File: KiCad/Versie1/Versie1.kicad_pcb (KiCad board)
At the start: 2 copper layers, 64 x 50 mm, 78 parts, among them IC1 MCP73831T-2ATI_OT, IC2 AP9221SA-CC-HAC-7, IC3 ISL91107IRTNZ-T7A, J1 Leftover, J2 USB_C_Receptacle_USB2.0, J3 JTAG, J4 Programmer, J5 SPI, J6 I2C, J7 BOOT, J8 Screw_Terminal_01x02, J9 Screw_Terminal_01x02, Q1 Q_NMOS_GSD, Q2 Q_NMOS_GSD, Q3 Q_NMOS_GSD, Q4 Q_NMOS_GSD, U1 ESP32-WROOM-32, Y1 32.768kHz

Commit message: H2, C13, C14 aangepast
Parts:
- moved H2 13.5 mm to (109.5, 87.6)
- moved C13 4.49 mm to (113.8, 87.1)
- moved JP5 3.59 mm to (96.0, 89.7)
- moved JP3 3.56 mm to (104.4, 89.3)
- moved JP4 3.53 mm to (100.7, 89.7)
- moved C14 3.26 mm to (113.8, 83.7)
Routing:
- net SPI_MOSI: track 56.1 -> 46.1 mm
- net I2C_SDA: track 38.4 -> 32.7 mm
- net SPI_MISO: track 33.4 -> 28.5 mm
- net I2C_SCL: track 40.5 -> 36.4 mm
- net SPI_CLK: track 24.0 -> 20.4 mm
- net GND: track 74.7 -> 71.5 mm, vias 52 -> 48
- net SCL\SCK\RX: track 49.8 -> 53.1 mm
- net +3V3: track 252.6 -> 249.9 mm
- net +BATT: track 137.2 -> 135.7 mm, vias 2 -> 3
- net uC_SENSE: track 41.6 -> 42.9 mm
- net SDA\MISO\TX: track 42.4 -> 43.7 mm

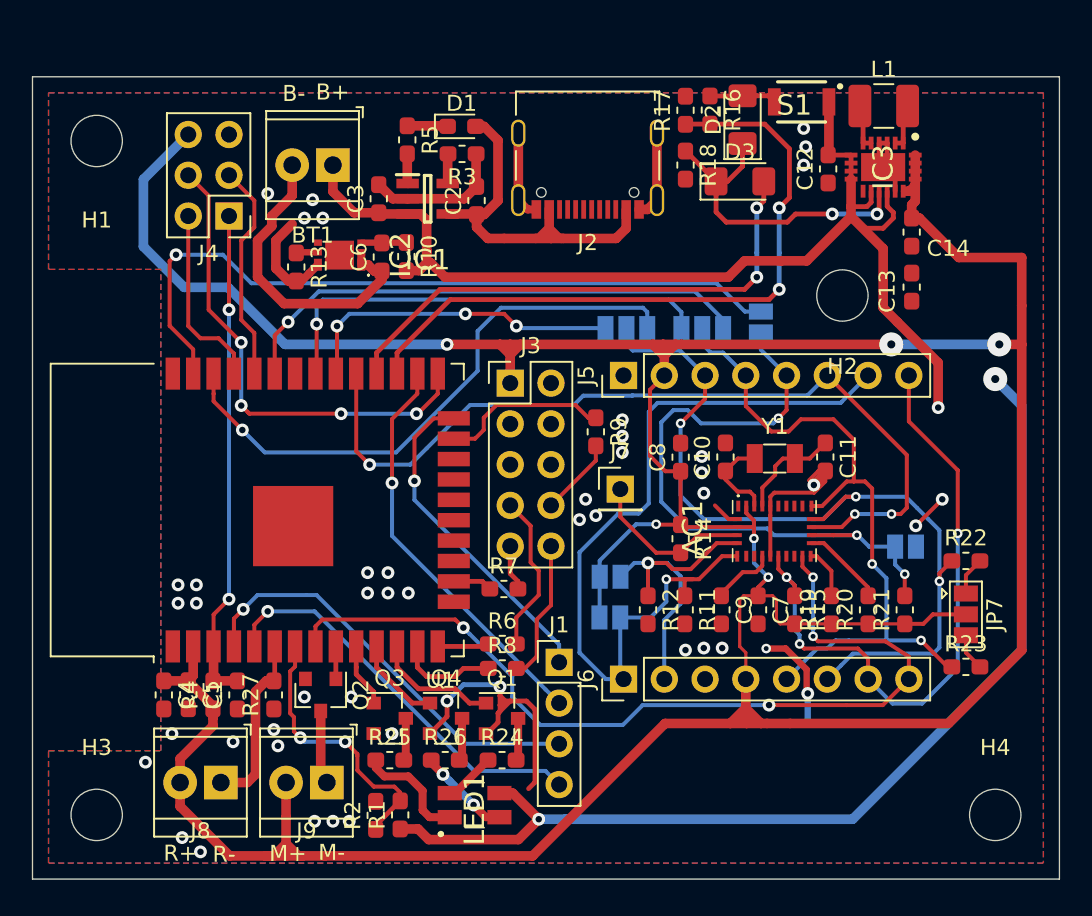
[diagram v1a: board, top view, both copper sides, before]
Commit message: 5x6cm PCB en silkscreen update
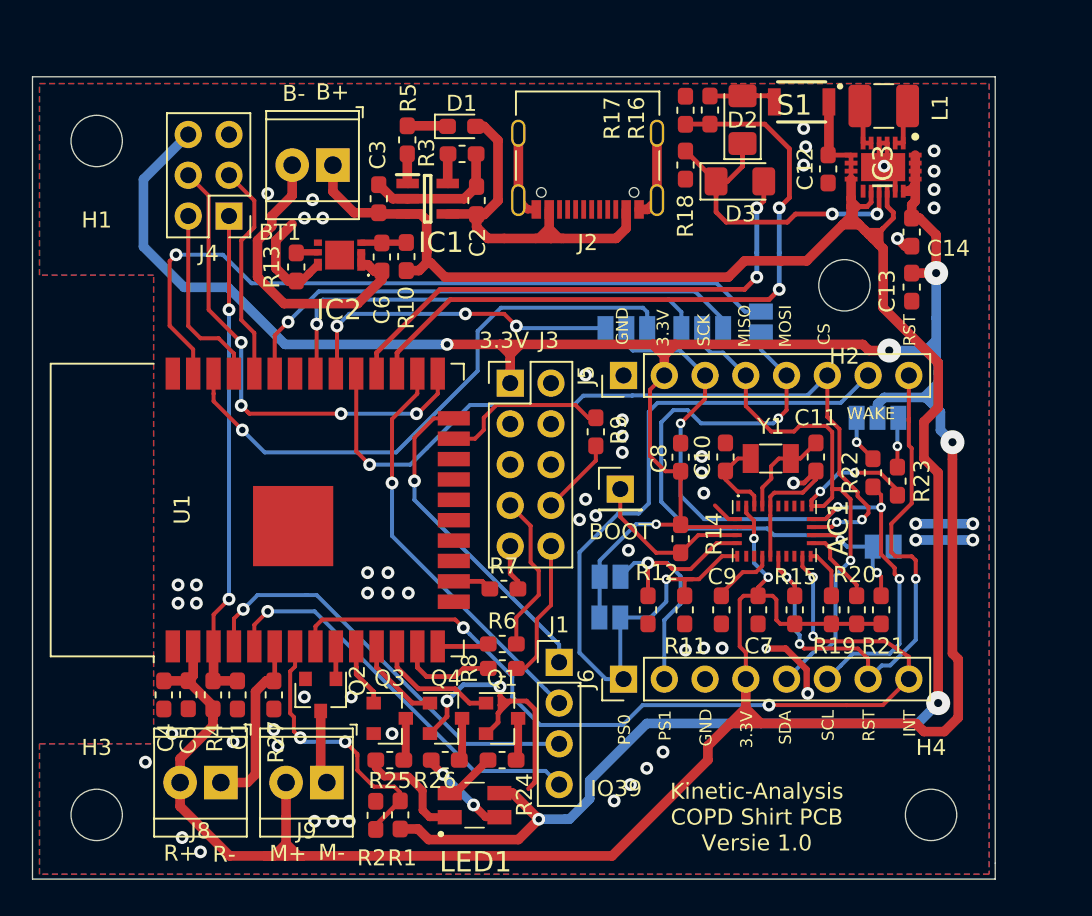
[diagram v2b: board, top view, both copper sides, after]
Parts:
- JP7: moved to B.Cu
- moved JP7 13.4 mm to (111.7, 95.2), turned to 0 degrees
- moved R23 12.3 mm to (112.9, 99.2), turned to 90 degrees
- moved R22 7.98 mm to (111.4, 98.7), turned to 90 degrees
- moved H4 4.00 mm to (115.0, 120.0)
- moved R21 1.47 mm to (111.9, 107.2)
- moved JP6 1.40 mm to (112.0, 103.3)
- moved R20 0.71 mm to (110.4, 107.2)
- moved H2 0.65 mm to (109.6, 87.0)
- moved C11 0.59 mm to (107.8, 97.7)
- moved Y1 0.25 mm to (105.0, 97.8)
- renumbered J7 to BOOT
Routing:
- net SCL\SCK\RX: track 53.1 -> 46.1 mm, vias 3 -> 4
- net RST: track 39.9 -> 35.8 mm
- net +3V3: track 249.9 -> 245.9 mm, vias 6 -> 7
- net SDA\MISO\TX: track 43.7 -> 40.2 mm, vias 2 -> 3
- net SPI_CS: track 53.6 -> 50.4 mm
- net GND: track 71.5 -> 74.1 mm, vias 48 -> 62
- net ADDR\MOSI: track 41.2 -> 38.8 mm
- net +BATT: track 135.7 -> 137.5 mm, vias 3 -> 2
- net Net-(JP7-Pad3): track 2.39 -> 3.10 mm, vias 0 -> 1
- net Net-(JP7-Pad1): track 2.39 -> 2.97 mm, vias 0 -> 1
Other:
- board size 64 x 50 mm -> 60 x 50 mm
- rule trace_min: 0.1 -> 0.25
- rule via_min_size: 0.4 -> 0.3
- board text added: "3.3V"
- board text added: "CS"
- board text added: "GND"
- board text added: "INT"
- board text added: "IO39"
- board text added: "Kinetic-Analysis COPD Shirt PCB Versie 1.0"
- board text added: "MISO"
- board text added: "MOSI"
- board text added: "PS0"
- board text added: "PS1"
- board text added: "RST"
- board text added: "SCK"
- board text added: "SCL"
- board text added: "SDA"
- board text added: "WAKE"

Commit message: BOM Lijst
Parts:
- removed the IC1 at (83.6, 81.6)
- removed the R3 at (85.8, 78.8)
- removed the R5 at (82.4, 77.9)
- added R8: 470, Resistor_SMD:R_0603_1608Metric_Pad1.05x0.95mm_HandSolder, F.Cu at (85.2, 80.8)
- added R9: 2k, Resistor_SMD:R_0603_1608Metric_Pad1.05x0.95mm_HandSolder, F.Cu at (85.2, 82.3)
- added U2: , Versie1_FootprintLib:MCP73831T-2ATI&slash_MC, F.Cu at (84.6, 78.0)
- C2, C3: value 4,7uF -> 4.7uF
- J2: value USB_C_Receptacle_USB2.0 -> USB_C_Receptacle_USB3.0
- moved C2 6.72 mm to (85.7, 75.1), turned to 0 degrees
- moved C3 4.64 mm to (82.7, 77.5), turned to 270 degrees
- moved D1 1.25 mm to (86.6, 78.0), turned to 90 degrees
- renumbered C7 to C6, C8 to C7, C6 to C8, IC2 to IC1, IC3 to IC2, BOOT to J7, R11 to R10, R12 to R11, R10 to R12, R14 to R13, R15 to R14, R13 to R15, R19 to R18, R18 to R19, R27 to R24, R24 to R25, R25 to R26, R26 to R27, R4 to R3, R6 to R4, R7 to R5, R8 to R6, R9 to R7
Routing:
- net +BATT: track 137.5 -> 148.4 mm
- net Net-(R9-Pad1): track 0.00 -> 3.66 mm
- net GND: track 74.1 -> 71.5 mm, vias 62 -> 64
- net Net-(IC1-Pad1): track 1.85 -> 0.00 mm
- net Net-(IC1-Pad5) (its old number): track 1.85 -> 0.00 mm
- net Net-(R8-Pad2): track 0.00 -> 1.61 mm
- net +5V: track 26.1 -> 25.0 mm
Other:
- board text added: "ESP_TXD"

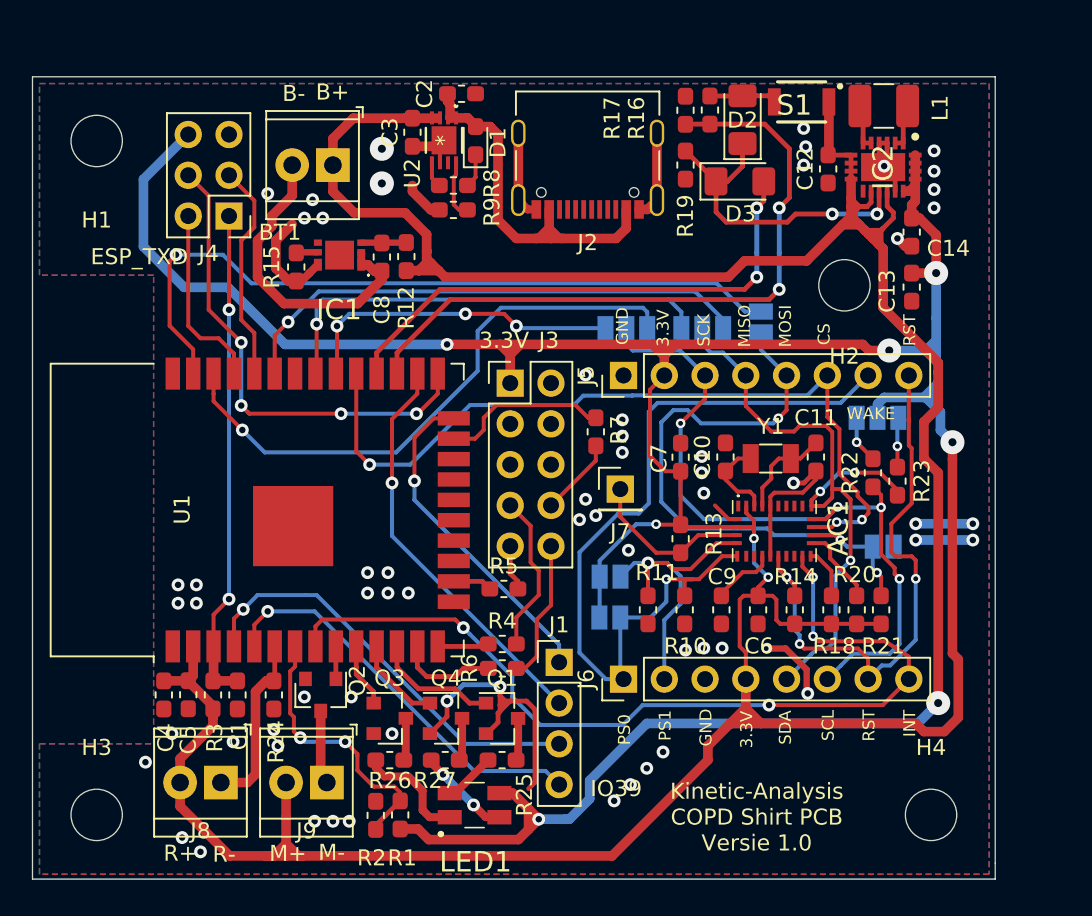
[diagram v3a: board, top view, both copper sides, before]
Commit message: IMU Footprint + Solder Jumper Power Latch
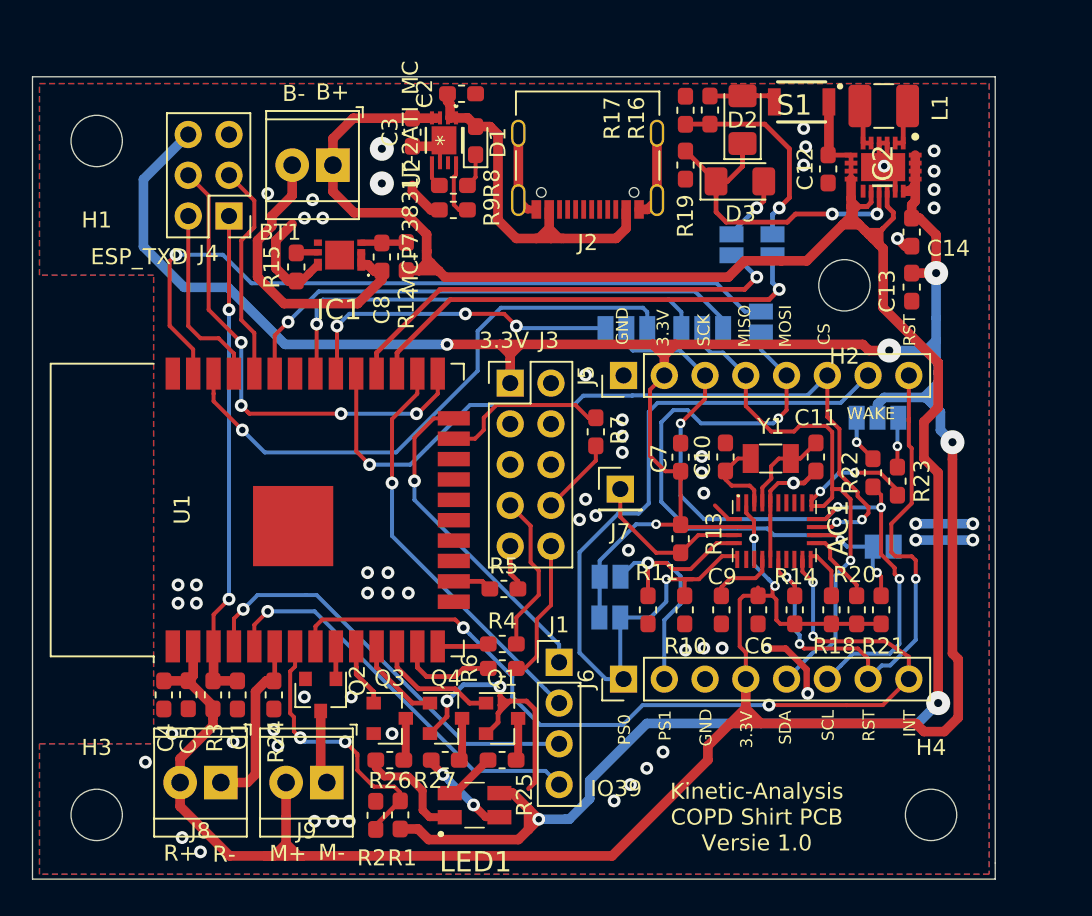
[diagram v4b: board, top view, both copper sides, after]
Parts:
- added JP8: SolderJumper_2_Open, Jumper:SolderJumper-2_P1.3mm_Open_Pad1.0x1.5mm, B.Cu at (102.6, 84.5)
- added JP9: SolderJumper_2_Open, Jumper:SolderJumper-2_P1.3mm_Open_Pad1.0x1.5mm, B.Cu at (105.1, 84.5)
- U2: value (none) -> MCP73831T-2ATI_MC
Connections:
- AC1 pad 1: (no net) -> Net-(AC1-Pad1)
- AC1 pad 12: (no net) -> Net-(AC1-Pad12)
- AC1 pad 13: (no net) -> Net-(AC1-Pad13)
- AC1 pad 21: (no net) -> Net-(AC1-Pad21)
- AC1 pad 22: (no net) -> Net-(AC1-Pad22)
- AC1 pad 23: (no net) -> Net-(AC1-Pad23)
- AC1 pad 24: (no net) -> Net-(AC1-Pad24)
- AC1 pad 7: (no net) -> Net-(AC1-Pad7)
- AC1 pad 8: (no net) -> Net-(AC1-Pad8)
- D3 pad 2: uC_LATCH -> LATCH
- IC1 pad 4: (no net) -> Net-(IC1-Pad4)
- IC1 pad 7: (no net) -> Net-(IC1-Pad7)
- IC2 pad 11: (no net) -> Net-(IC2-Pad11)
- J2 pad A5: (no net) -> Net-(J2-PadA5)
- J2 pad A6: (no net) -> Net-(J2-PadA6)
- J2 pad A7: (no net) -> Net-(J2-PadA7)
- J2 pad A8: (no net) -> Net-(J2-PadA8)
- J2 pad B5: (no net) -> Net-(J2-PadB5)
- J2 pad B6: (no net) -> Net-(J2-PadB6)
- J2 pad B7: (no net) -> Net-(J2-PadB7)
- J2 pad B8: (no net) -> Net-(J2-PadB8)
- J3 pad 6: (no net) -> Net-(J3-Pad6)
- R16 pad 2: uC_SENSE -> SENSE
- R17 pad 1: uC_SENSE -> SENSE
- U1 pad 17: (no net) -> Net-(U1-Pad17)
- U1 pad 18: (no net) -> Net-(U1-Pad18)
- U1 pad 19: (no net) -> Net-(U1-Pad19)
- U1 pad 20: (no net) -> Net-(U1-Pad20)
- U1 pad 21: (no net) -> Net-(U1-Pad21)
- U1 pad 22: (no net) -> Net-(U1-Pad22)
- U1 pad 32: (no net) -> Net-(U1-Pad32)
- U2 pad 7: (no net) -> Net-(U2-Pad7)
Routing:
- net uC_SENSE: track 42.9 -> 29.1 mm, vias 2 -> 1
- net SENSE: track 0.00 -> 12.9 mm, vias 0 -> 1
- net LATCH: track 0.00 -> 4.13 mm, vias 0 -> 1
- net uC_LATCH: track 33.1 -> 29.1 mm, vias 2 -> 1
- net GND: track 71.5 -> 70.0 mm
- net Net-(AC1-Pad9): track 4.01 -> 4.98 mm
- net Net-(AC1-Pad27): track 5.27 -> 5.91 mm
- net +3V3: track 245.9 -> 246.4 mm
